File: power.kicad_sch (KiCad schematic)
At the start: 33 parts, among them U1 SF32LB525UC6, U2 BQ27426YZFR, U3 TPS25200DRVT

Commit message: save progress before refactor
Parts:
- C1, C11, C12, C15, C16, C4: LCSC Part (none) -> C23733
- C10: footprint Capacitor_SMD:C_0402_1005Metric -> Capacitor_SMD:C_0603_1608Metric; LCSC Part (none) -> C1623
- C13, C9: LCSC Part (none) -> C52923
- C14, C3: LCSC Part (none) -> C12530
- C17, C18, C19, C7, C8: LCSC Part (none) -> C15525
- C2: value 0.47uF -> 470nF; footprint Capacitor_SMD:C_0402_1005Metric -> Capacitor_SMD:C_0603_1608Metric; LCSC Part (none) -> C1623
- C5: value 0.1uF -> 100nF; LCSC Part (none) -> C1525
- C6: footprint Capacitor_SMD:C_0402_1005Metric -> Capacitor_SMD:C_0603_1608Metric; LCSC Part (none) -> C59461
- L1: footprint Inductor_SMD:L_0603_1608Metric -> Inductor_SMD:L_0402_1005Metric; LCSC Part (none) -> C86065
- R1, R3: LCSC Part (none) -> C25744
- R2: LCSC Part (none) -> C159437
- R4, R6: footprint Resistor_SMD:R_0402_1005Metric -> Resistor_SMD:R_0603_1608Metric; LCSC Part (none) -> C23024
- R5: footprint Resistor_SMD:R_0402_1005Metric -> Resistor_SMD:R_0603_1608Metric; LCSC Part (none) -> C22807
- TP3, TP4, TP5: now left out of the parts list
- U1: LCSC Part (none) -> C47355842
- U2: LCSC Part (none) -> C165137
- U3: LCSC Part (none) -> C2653855

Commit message: finish up everything but nfc
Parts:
- BT1: footprint (none) -> custom_footprints:Generic_Solder_Pads_2P; now left out of the parts list
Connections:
- net FUEL_GPOUT: now reaches R3.2, U2.A1 (GPOUT)
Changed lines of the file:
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@@
 	(wire
 		(pts
-			(xy 57.15 120.65) (xy 58.42 120.65)
-		)
-		(stroke
-			(width 0)
-			(type default)
-		)
-	)
-	(wire
-		(pts
 			(xy 33.02 111.76) (xy 33.02 107.95)
 		)
@@
 	(wire
 		(pts
-			(xy 52.07 120.65) (xy 48.26 120.65)
-		)
-		(stroke
-			(width 0)
-			(type default)
-		)
-	)
-	(wire
-		(pts
 			(xy 154.94 66.04) (xy 154.94 68.58)
 		)
@@
 	(wire
 		(pts
-			(xy 48.26 120.65) (xy 48.26 116.84)
-		)
-		(stroke
-			(width 0)
-			(type default)
-		)
-	)
-	(wire
-		(pts
 			(xy 109.22 54.61) (xy 109.22 57.15)
 		)
@@
 	(wire
 		(pts
+			(xy 46.99 118.11) (xy 58.42 118.11)
+		)
+		(stroke
+			(width 0)
+			(type default)
+		)
+	)
+	(wire
+		(pts
 			(xy 217.17 101.6) (xy 219.71 101.6)
 		)
@@
 	(wire
 		(pts
+			(xy 58.42 120.65) (xy 58.42 118.11)
+		)
+		(stroke
+			(width 0)
+			(type default)
+		)
+	)
+	(wire
+		(pts
 			(xy 236.22 106.68) (xy 236.22 107.95)
 		)
@@
 		)
 	)
+	(global_label "FUEL_GPOUT"
+		(shape input)
+		(at 58.42 120.65 180)
+		(fields_autoplaced yes)
+		(effects
+			(font
+				(size 1.27 1.27)
+			)
+			(justify right)
+		)
+		(property "Intersheetrefs" "${INTERSHEET_REFS}"
+			(at 43.7024 120.65 0)
+			(effects
+				(font
+					(size 1.27 1.27)
+				)
+				(justify right)
+				(hide yes)
+			)
+		)
+	)
 	(global_label "OVP_FAULT"
 		(shape input)
@@
 			)
 		)
-		(property "Description" "Unpolarized capacitor, small symbol"
+		(property "Description" ""
 			(at 227.33 114.3 0)
 			(effects
@@
 	(symbol
 		(lib_id "power:+3V3")
-		(at 48.26 116.84 0)
+		(at 46.99 113.03 0)
 		(unit 1)
 		(exclude_from_sim no)
@@
 		(on_board yes)
 		(dnp no)
-		(fields_autoplaced yes)
 		(property "Reference" "#PWR09"
-			(at 48.26 120.65 0)
+			(at 46.99 116.84 0)
 			(effects
 				(font
@@
 		)
 		(property "Value" "+3V3"
-			(at 48.26 111.76 0)
+			(at 46.99 109.474 0)
 			(effects
 				(font
@@
 		)
 		(property "Footprint" ""
-			(at 48.26 116.84 0)
+			(at 46.99 113.03 0)
 			(effects
 				(font
@@
 		)
 		(property "Datasheet" ""
-			(at 48.26 116.84 0)
+			(at 46.99 113.03 0)
 			(effects
 				(font
@@
 		)
 		(property "Description" "Power symbol creates a global label with name \"+3V3\""
-			(at 48.26 116.84 0)
+			(at 46.99 113.03 0)
 			(effects
 				(font
@@
 			)
 		)
-		(property "Description" "Unpolarized capacitor, small symbol"
+		(property "Description" ""
 			(at 246.38 81.28 0)
 			(effects
@@
 	)
 	(symbol
+		(lib_id "Device:R_Small")
+		(at 46.99 115.57 0)
+		(unit 1)
+		(exclude_from_sim no)
+		(in_bom yes)
+		(on_board yes)
+		(dnp no)
+		(property "Reference" "R3"
+			(at 48.514 114.3 0)
+			(effects
+				(font
+					(size 1.016 1.016)
+				)
+				(justify left)
+			)
+		)
+		(property "Value" "10k"
+			(at 48.514 116.84 0)
+			(effects
+				(font
+					(size 1.27 1.27)
+				)
+				(justify left)
+			)
+		)
+		(property "Footprint" "Resistor_SMD:R_0402_1005Metric"
+			(at 46.99 115.57 0)
+			(effects
+				(font
+					(size 1.27 1.27)
+				)
+				(hide yes)
+			)
+		)
+		(property "Datasheet" "~"
+			(at 46.99 115.57 0)
+			(effects
+				(font
+					(size 1.27 1.27)
+				)
+				(hide yes)
+			)
+		)
+		(property "Description" "Resistor, small symbol"
+			(at 46.99 115.57 0)
+			(effects
+				(font
+					(size 1.27 1.27)
+				)
+				(hide yes)
+			)
+		)
+		(property "LCSC Part" "C25744"
+			(at 46.99 115.57 0)
+			(effects
+				(font
+					(size 1.27 1.27)
+				)
+				(hide yes)
+			)
+		)
+		(pin "2"
+		)
+		(pin "1"
+		)
+		(instances
+			(project ""
+				(path "/c6cb5a1d-9f97-4766-8582-a9e93ed049e4/c8f10ca5-34ba-4d6f-bc46-aa895fb40a01"
+					(reference "R3")
+					(unit 1)
+				)
+			)
+		)
+	)
+	(symbol
 		(lib_id "Device:C_Small")
 		(at 232.41 130.81 0)
@@
 	)
 	(symbol
-		(lib_id "Device:R_Small")
-		(at 54.61 120.65 90)
-		(unit 1)
-		(exclude_from_sim no)
-		(in_bom yes)
-		(on_board yes)
-		(dnp no)
-		(property "Reference" "R3"
-			(at 54.61 118.618 90)
-			(effects
-				(font
-					(size 1.016 1.016)
-				)
-			)
-		)
-		(property "Value" "10k"
-			(at 54.61 122.936 90)
-			(effects
-				(font
-					(size 1.27 1.27)
-				)
-			)
-		)
-		(property "Footprint" "Resistor_SMD:R_0402_1005Metric"
-			(at 54.61 120.65 0)
-			(effects
-				(font
-					(size 1.27 1.27)
-				)
-				(hide yes)
-			)
-		)
-		(property "Datasheet" "~"
-			(at 54.61 120.65 0)
-			(effects
-				(font
-					(size 1.27 1.27)
-				)
-				(hide yes)
-			)
-		)
-		(property "Description" "Resistor, small symbol"
-			(at 54.61 120.65 0)
-			(effects
-				(font
-					(size 1.27 1.27)
-				)
-				(hide yes)
-			)
-		)
-		(property "LCSC Part" "C25744"
-			(at 54.61 120.65 90)
-			(effects
-				(font
-					(size 1.27 1.27)
-				)
-				(hide yes)
-			)
-		)
-		(pin "2"
-		)
-		(pin "1"
-		)
-		(instances
-			(project ""
-				(path "/c6cb5a1d-9f97-4766-8582-a9e93ed049e4/c8f10ca5-34ba-4d6f-bc46-aa895fb40a01"
-					(reference "R3")
-					(unit 1)
-				)
-			)
-		)
-	)
-	(symbol
 		(lib_id "power:GND")
 		(at 43.18 152.4 0)
@@
 		(unit 1)
 		(exclude_from_sim no)
-		(in_bom yes)
+		(in_bom no)
 		(on_board yes)
 		(dnp no)
@@
 			)
 		)
-		(property "Footprint" ""
+		(property "Footprint" "custom_footprints:Generic_Solder_Pads_2P"
 			(at 43.18 145.796 90)
 			(effects
@@
 			)
 		)
-		(property "Description" "Unpolarized capacitor, small symbol"
+		(property "Description" ""
 			(at 154.94 134.62 0)
 			(effects
@@
 			)
 		)
-		(property "Description" "Unpolarized capacitor, small symbol"
+		(property "Description" ""
 			(at 226.06 58.42 0)
 			(effects
@@
 			)
 		)
-		(property "Description" "Unpolarized capacitor, small symbol"
+		(property "Description" ""
 			(at 222.25 96.52 0)
 			(effects
@@
 			)
 		)
-		(property "Description" "Unpolarized capacitor, small symbol"
+		(property "Description" ""
 			(at 222.25 101.6 0)
 			(effects

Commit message: hopefully final schematic before splitting out
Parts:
- removed C2: 470nF, Capacitor_SMD:C_0603_1608Metric, symbol Device:C_Small
- removed C3: 2.2uF, Capacitor_SMD:C_0402_1005Metric, symbol Device:C_Small
- removed C9: 1uF, Capacitor_SMD:C_0402_1005Metric, symbol Device:C_Small
- removed R1, R3: 10k, Resistor_SMD:R_0402_1005Metric, symbol Device:R_Small
- removed R2: 0.01, Resistor_SMD:R_1206_3216Metric, symbol Device:R_Small
- removed U2: BQ27426YZFR, BQ27426:YZF0009AKAL, symbol 2026-03-01_07-06-16:BQ27426YZFR
- renumbered C15 to C10, C14 to C11, C13 to C12, C12 to C13, C11 to C14, C10 to C15, C18 to C16, C1 to C17, C17 to C18, C16 to C19, C19 to C20, C4 to C21, C5 to C6, C6 to C7, C7 to C9, L1 to L3, R4 to R5, R5 to R7, TP4 to TP10, TP5 to TP11, TP3 to TP9
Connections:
- net VBAT: now also BT1.1 (+), TP9.1
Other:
- moved on the sheet: BT1, C10, C11, C12, C13, C14, C15, C16, C17, C18, C19, C20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

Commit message: final review, fixes, cleanup
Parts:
- removed TP11: 3V3, TestPoint:TestPoint_Pad_D1.0mm, symbol Connector:TestPoint_Small
- added D4: ESD5341N, Diode_SMD:D_SOD-882, symbol Device:D_Zener_Small
- added TP11: 3V3, TestPoint:TestPoint_Pad_D1.0mm, symbol Connector:TestPoint
- C11: LCSC Part C12530 -> C1559
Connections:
- net +3V3: now also TP11.1
- net +3V3_G1: no longer C20.1, U1.22 (VDD33_VOUT1)
- net GND: now also D4.1 (K)
- net VBUS_RAW: now also D4.2 (A)
- new net: C20.1, U1.22 (VDD33_VOUT1)
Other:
- moved on the sheet: BT1, C10, C11, C12, C13, C14, C15, C16, C17, C18, C19, C20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

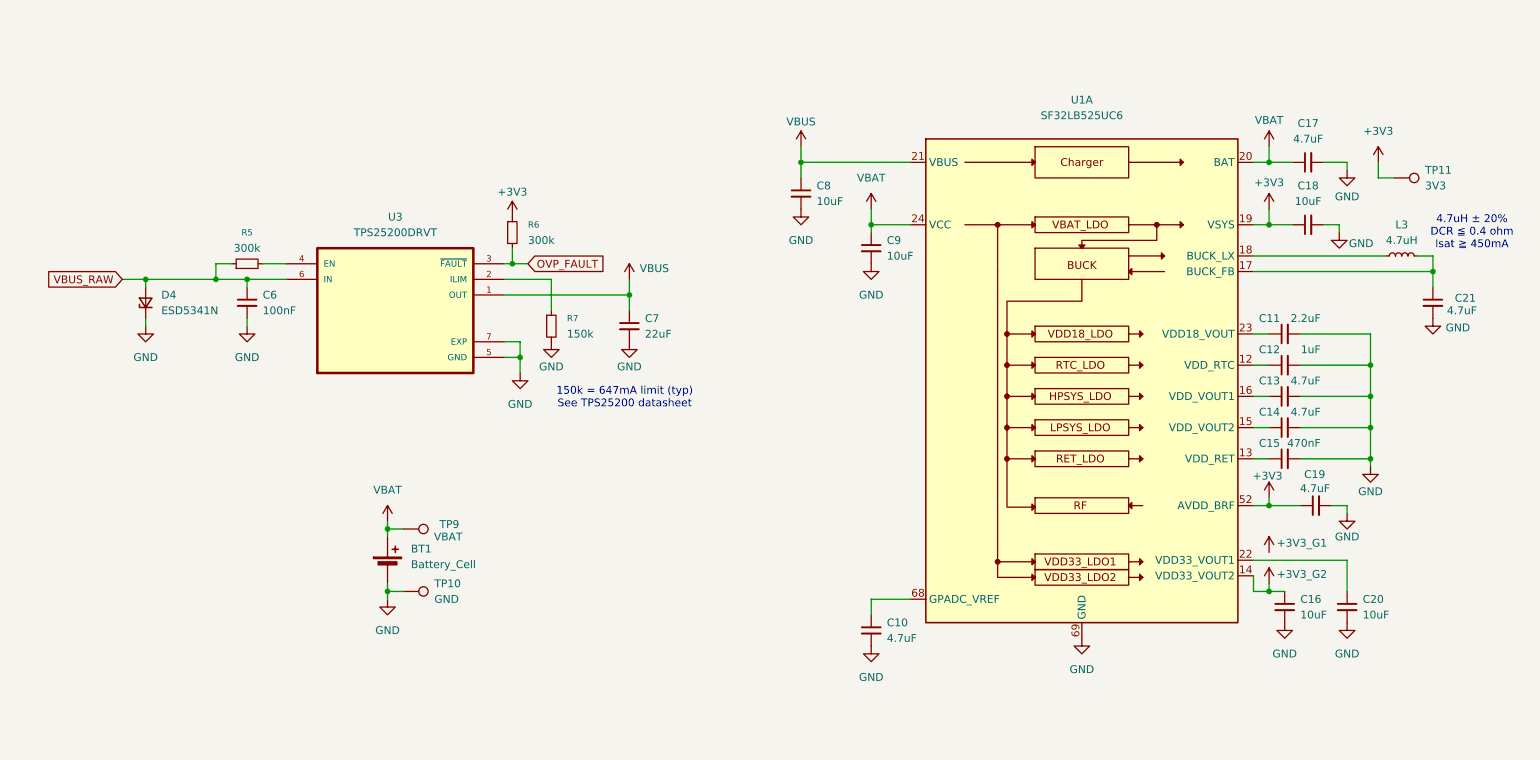
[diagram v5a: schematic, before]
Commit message: prepare schematic for devboard
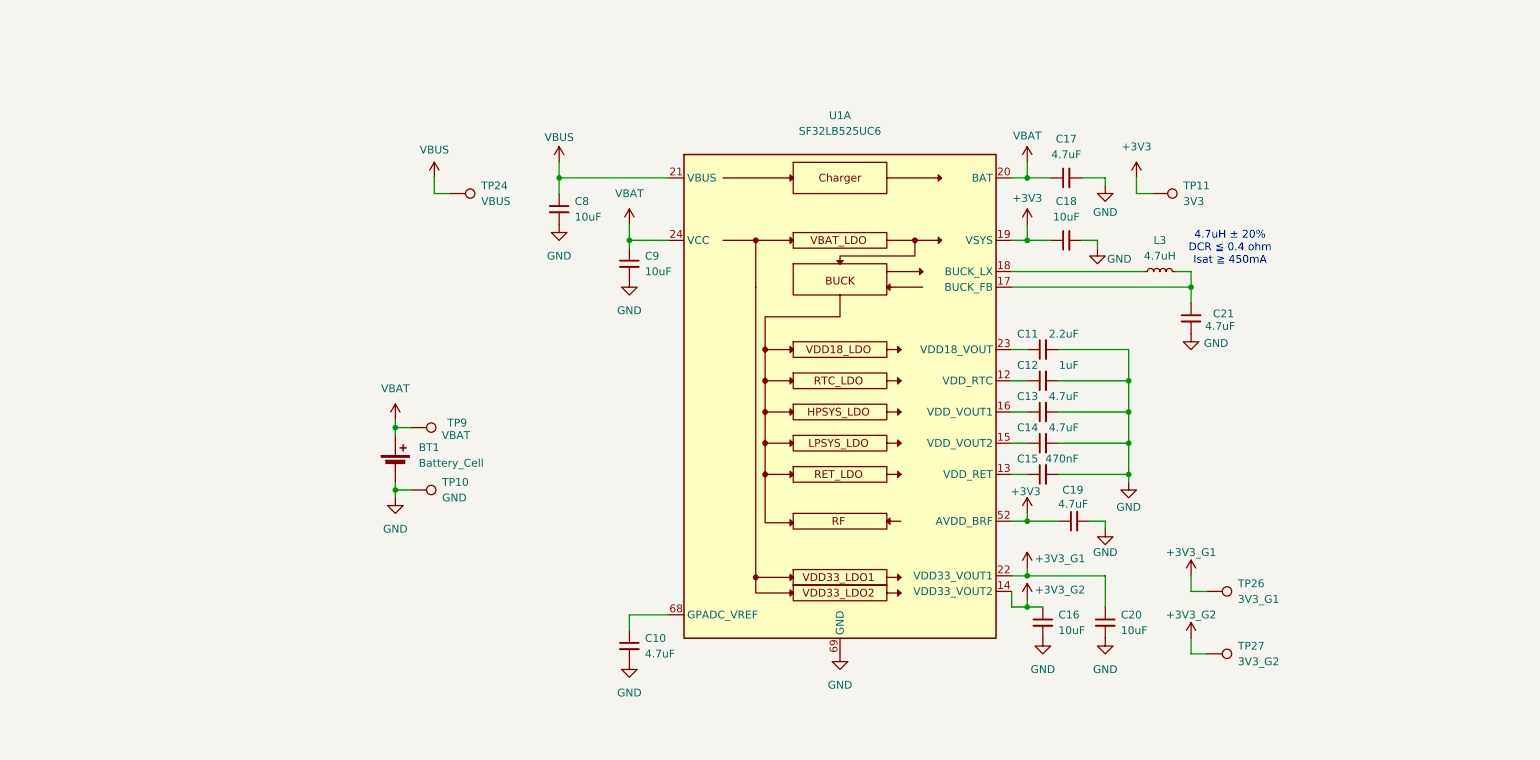
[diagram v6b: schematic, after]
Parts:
- removed C6: 100nF, Capacitor_SMD:C_0402_1005Metric, symbol Device:C_Small
- removed C7: 22uF, Capacitor_SMD:C_0603_1608Metric, symbol Device:C_Small
- removed D4: ESD5341N, Diode_SMD:D_SOD-882, symbol Device:D_Zener_Small
- removed R5, R6: 300k, Resistor_SMD:R_0603_1608Metric, symbol Device:R_Small
- removed R7: 150k, Resistor_SMD:R_0603_1608Metric, symbol Device:R_Small
- removed U3: TPS25200DRVT, TPS25200DRVT:SON65P200X200X80-7N, symbol TPS25200DRVT:TPS25200DRVT
- added TP24: VBUS, TestPoint:TestPoint_Pad_D1.0mm, symbol Connector:TestPoint
- added TP26: 3V3_G1, TestPoint:TestPoint_Pad_D1.0mm, symbol Connector:TestPoint
- added TP27: 3V3_G2, TestPoint:TestPoint_Pad_D1.0mm, symbol Connector:TestPoint
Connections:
- net +3V3_G1: now also C20.1, U1.22 (VDD33_VOUT1), TP26.1
- net +3V3_G2: now also TP27.1
- net VBUS: now also TP24.1
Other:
- note removed: "150k = 647mA limit (typ) See TPS25200 datasheet"
- moved on the sheet: BT1, C10, C11, C12, C13, C14, C15, C16, C17, C18, C19, C20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

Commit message: huge progress on bentoboard, schematic fixes
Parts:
- C15: footprint Capacitor_SMD:C_0603_1608Metric -> Capacitor_SMD:C_0402_1005Metric; LCSC Part C1623 -> C47339
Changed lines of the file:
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@@
 			)
 		)
-		(property "Footprint" "Capacitor_SMD:C_0603_1608Metric"
+		(property "Footprint" "Capacitor_SMD:C_0402_1005Metric"
 			(at 190.5 114.3 0)
 			(effects
@@
 			)
 		)
-		(property "LCSC Part" "C1623"
+		(property "LCSC Part" "C47339"
 			(at 190.5 114.3 90)
 			(effects

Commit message: revise some decoupling caps to be 0201
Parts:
- C11: footprint Capacitor_SMD:C_0402_1005Metric -> Capacitor_SMD:C_0201_0603Metric; LCSC Part C1559 -> C77762
- C12: footprint Capacitor_SMD:C_0402_1005Metric -> Capacitor_SMD:C_0201_0603Metric; LCSC Part C52923 -> C53067
- C13, C14: footprint Capacitor_SMD:C_0402_1005Metric -> Capacitor_SMD:C_0201_1005Metric; LCSC Part C23733 -> C335103
- C15: footprint Capacitor_SMD:C_0402_1005Metric -> Capacitor_SMD:C_0201_0603Metric; LCSC Part C47339 -> C85926
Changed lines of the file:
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@@
 			)
 		)
-		(property "Footprint" "Capacitor_SMD:C_0402_1005Metric"
+		(property "Footprint" "Capacitor_SMD:C_0201_0603Metric"
 			(at 190.5 99.06 0)
 			(effects
@@
 			)
 		)
-		(property "LCSC Part" "C52923"
+		(property "LCSC Part" "C53067"
 			(at 190.5 99.06 90)
 			(effects
@@
 			)
 		)
-		(property "Footprint" "Capacitor_SMD:C_0402_1005Metric"
+		(property "Footprint" "Capacitor_SMD:C_0201_0603Metric"
 			(at 190.5 93.98 0)
 			(effects
@@
 			)
 		)
-		(property "LCSC Part" "C1559"
+		(property "LCSC Part" "C77762"
 			(at 190.5 93.98 90)
 			(effects
@@
 			)
 		)
-		(property "Footprint" "Capacitor_SMD:C_0402_1005Metric"
+		(property "Footprint" "Capacitor_SMD:C_0201_0603Metric"
 			(at 190.5 114.3 0)
 			(effects
@@
 			)
 		)
-		(property "LCSC Part" "C47339"
+		(property "LCSC Part" "C85926"
 			(at 190.5 114.3 90)
 			(effects
@@
 			)
 		)
-		(property "Footprint" "Capacitor_SMD:C_0402_1005Metric"
+		(property "Footprint" "Capacitor_SMD:C_0201_1005Metric"
 			(at 190.5 104.14 0)
 			(effects
@@
 			)
 		)
-		(property "LCSC Part" "C23733"
+		(property "LCSC Part" "C335103"
 			(at 190.5 104.14 90)
 			(effects
@@
 			)
 		)
-		(property "Footprint" "Capacitor_SMD:C_0402_1005Metric"
+		(property "Footprint" "Capacitor_SMD:C_0201_1005Metric"
 			(at 190.5 109.22 0)
 			(effects
@@
 			)
 		)
-		(property "LCSC Part" "C23733"
+		(property "LCSC Part" "C335103"
 			(at 190.5 109.22 90)
 			(effects
